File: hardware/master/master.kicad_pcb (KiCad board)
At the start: 2 copper layers, 68 x 54 mm, 34 parts, among them J1 5V IN, J2 BUS OUT, J3 IO RSV, J4 STEP-UP 5V->15V, U1 ESP32-C3 SuperMini, U2 TP8485E-SR, U3 74LVC1G17

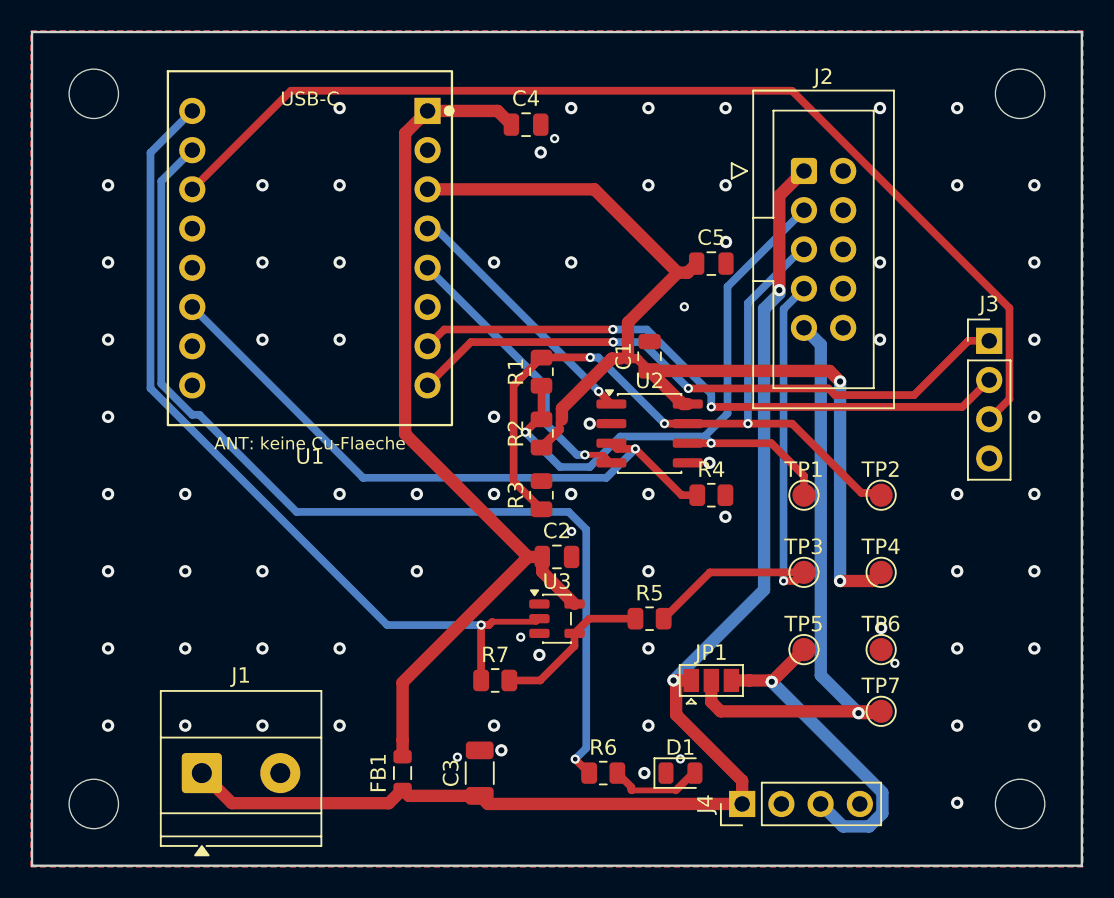
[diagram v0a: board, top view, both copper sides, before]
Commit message: Master: Symbolpruefung freigegeben (M-1), 3D-Renders
- docs/symbolpruefung-master.md: M-1 + 74LVC1G17 vom Betreiber freigegeben
  (01.09.2026). ESP32-C3-Pinbelegung/Einbaulage als geprueft markiert.
- tools/gen_master_pcb.py --render: kicad-cli pcb render (oben/unten) ->
  docs/render-master-{top,bottom}.png fuer die Sichtkontrolle der
  U1-Einbaulage (Pin-1 = 5V rechts oben, "USB-C" oben, "ANT" unten).
- Hinweis zur USB-C-Buchse: Modulkoerper endet ~2,7 mm vor der Oberkante;
  weiter hochsetzen sprengt den Routingkanal -> im GUI Edge.Cuts-Aussparung.
- docs/{schaltplan,layout,projektstand,backlog} nachgezogen.

Co-Authored-By: Claude Sonnet 5 <noreply@anthropic.com>
Claude-Session: https://claude.ai/code/session_01UsXTvE3jGgoK5Hec7hVbyD
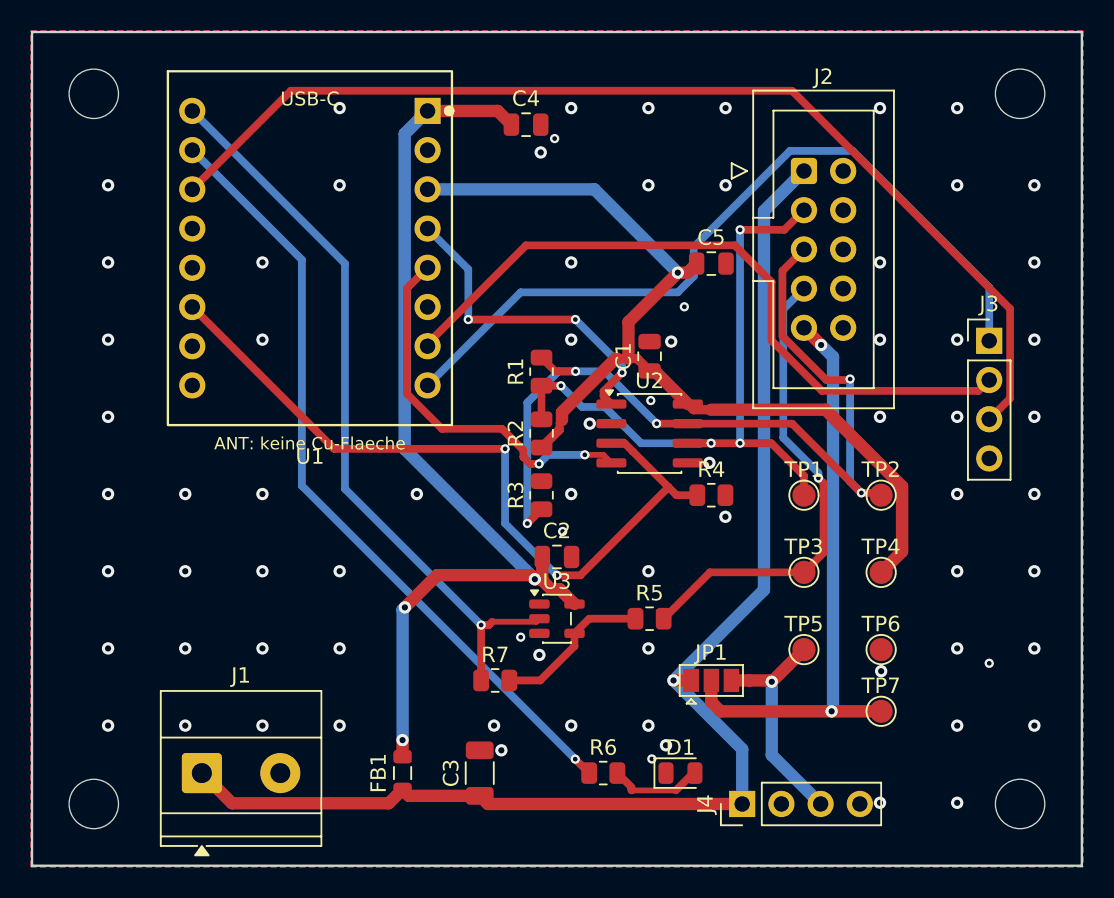
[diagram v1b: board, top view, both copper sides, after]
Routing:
- net /LED_DRV: track 63.8 -> 51.0 mm
- net /IO0_RSV: track 40.4 -> 50.9 mm, vias 2 -> 0
- net /DE: track 41.0 -> 50.2 mm, vias 1 -> 2
- net /RS485_B: track 49.9 -> 58.2 mm, vias 3 -> 5
- net /+15V: track 22.0 -> 14.8 mm
- net /+3V3: track 69.0 -> 62.7 mm, vias 2 -> 1
- net /DI: track 18.6 -> 24.6 mm, vias 1 -> 2
- net /CHAIN_GPIO: track 54.4 -> 48.6 mm
- net /IO1_RSV: track 40.1 -> 45.6 mm, vias 2 -> 0
- net /RO: track 16.6 -> 21.4 mm, vias 1 -> 3
- net /+5V: track 59.7 -> 64.1 mm, vias 0 -> 3
- net /ADER9: track 40.6 -> 38.3 mm, vias 1 -> 2
- net /RS485_A: track 44.5 -> 42.8 mm, vias 2 -> 4
- net /+5V_IN: track 84.0 -> 84.1 mm, vias 2 -> 1
- net /GND: vias 76 -> 75

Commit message: Master-Traegerboard Rev. 0.2: Verpolschutz + RS-485-TVS am Eingang
Vor der PCB-Bestellung nachgeruestet (Betreiber-Entscheidungen 10.09.2026):

- Q1 (AO3401A, P-Kanal, High-Side) + R8 (100k V_GS) = Verpolschutz am
  5-V-Eingang, direkt hinter J1 und VOR der J2-Abzweigung -> schuetzt bei
  vertauschter Klemme die gesamte Kette. Neues Netz +5V_RAW (J1->Q1).
- D2 (SM712 / PSM712-LF-T7) = RS-485-TVS-Array zwischen A/B und GND,
  7 V / 12 V asymmetrisch (RS-485-Gleichtakt -7..+12 V). Pinbelegung gegen
  das Bourns-CDSOT23-SM712-Datenblatt geprueft (Pin 3 = GND).
- Alle drei sind LCSC-Basic-Teile: C15127, C149504, C32677.
- M-3 entschieden: U3 (74LVC1G17) wird bestueckt, R7 (0R) bleibt DNP-Reserve.
- Keine Edge.Cuts-Aussparung fuer U1 -- das Modul steckt in Buchsenleisten
  und wird zum Flashen entnommen.
- 5-V- und 42-V~-Kreis bleiben vollstaendig galvanisch getrennt (eigenes
  5-V-Netzteil, kein gemeinsamer Trafo, 5 V nicht aus den 42 V~).

Werkzeuge:
- build_krone_master_symbols.py: AO3401A + SM712_SOT23 aus der KiCad-Lib.
- gen_master_sch.py / gen_master_pcb.py: Q1/R8/D2 in Netzliste + PLACEMENT
  (PLACEMENT akzeptiert jetzt opt. Rueckseiten-Flag).
- tools/patch_master_pcb.py (neu): setzt neue Bauteile inkrementell in die
  geroutete Platine ein und schliesst nur die neuen Verbindungen mit
  finish_routes.py -- FreeRouting 2.3.0 haengt in dieser Umgebung reproduzierbar.
- route_master.py / route_daughtercard.py: -Dfreerouting.gui.enabled=false +
  Popen-Watchdog (.ses-Stabilitaet / CPU-Stillstand) + 3 Anlaeufe, --passes 6.

ERC 0/0, DRC 0/0. Schaltplan Rev. 0.2, Fertigungspaket regeneriert (18 SMD).
docs/schaltplan-master.md, symbolpruefung-master.md (AO3401A + SM712, M-4),
layout-master.md, spezifikation.md v0.21, backlog T20, projektstand, toolchain.

Co-Authored-By: Claude Sonnet 5 <noreply@anthropic.com>
Claude-Session: https://claude.ai/code/session_01UsXTvE3jGgoK5Hec7hVbyD
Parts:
- added D2: SM712, SOT-23, F.Cu at (46.0, 33.0)
- added Q1: AO3401A, SOT-23, F.Cu at (16.0, 40.0)
- added R8: 100k, R_0805_2012Metric, F.Cu at (20.0, 40.0)
- moved GH1 13.0 mm to (34.0, 25.0)
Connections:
- J1 pad 1: /+5V_IN -> /+5V_RAW
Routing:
- net /+5V_RAW: track 0.00 -> 15.5 mm, vias 0 -> 2
- net /RS485_B: track 58.2 -> 69.9 mm, vias 5 -> 9
- net /+5V_IN: track 84.1 -> 92.9 mm
- net /RS485_A: track 42.8 -> 48.4 mm, vias 4 -> 5
- net /GND: vias 75 -> 78

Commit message: Master Rev. 0.2: Silk -- "ANT"-Text raus, + / - an J1; Symbolpruefung frei
Betreiber-Rueckmeldung zur PCB:
- "ANT: keine Cu-Flaeche" vom U1-Footprint entfernt (der Kupfer-Keepout
  unter der Antenne bleibt). .kicad_mod bereinigt; patch_master_pcb.py
  entfernt den im Board eingebackenen Text zusaetzlich.
- + / - auf F.SilkS links/rechts neben J1 (links = +5V, rechts = GND).
  Neue Funktion add_power_terminal_polarity() in add_silk_marks.py, nur
  fuer 2-polige Klemmen (die 2x5-Buchsenleiste der Daughter Card bleibt
  unberuehrt).
- patch_master_pcb.py: finish_routes jetzt in bis zu 4 Runden (A*-Suche
  nicht deterministisch).

Symbolpruefung-master.md: AO3401A + SM712/PSM712 vom Betreiber freigegeben,
M-3 und M-4 geschlossen.

ERC 0/0, DRC 0/0 (3 kosmetische Silk-Warnungen: Referenztext D2/U2/R4 --
im GUI zu bereinigen). Fertigungspaket + Renders regeneriert.

Co-Authored-By: Claude Sonnet 5 <noreply@anthropic.com>
Claude-Session: https://claude.ai/code/session_01UsXTvE3jGgoK5Hec7hVbyD
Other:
- board text added: "+"
- board text added: "−"
